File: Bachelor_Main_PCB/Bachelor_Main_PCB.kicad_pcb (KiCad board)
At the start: 4 copper layers, 216 parts, among them IC1 LD3985M18R, J1 M20-9990245, J11 F32Q-1A7H1-11022, J13 CONMHF1-SMD-G-T, J14 CONMHF1-SMD-G-T, J2 M20-9990245, J21 CONMHF1-SMD-G-T, J25 M20-9990245, J26 691137710002, J27 Conn_01x03_Pin, J28 691137710002, J29 M20-9990245, J4 MEM2075-00-140-01-A, J8 Conn_01x07_Pin, J9 M20-9990245, P1 SF70S006VBAR2000, Q1 SSM3J358R,LF, Q10 NX3008NBKW, Q11 SSM3J358R,LF, Q12 NX3008NBKW, Q13 BC817-40Q-13-F, Q2 SSM3J358R,LF, Q3 NX3008NBKW, Q4 NX3008NBKW, Q5 NX3008NBKW, Q6 NX3008NBKW, Q7 NX3008NBKW, Q8 NX3008NBKW, Q9 NX3008NBKW, U1 USB3320C-EZK-TR, U10 LMR51450FNDRRR, U11 USB2514B-I/M2, U2 STM32H7A3ZITxQ, U3 ESD7004MUTAG, U4 ESD7004MUTAG, U5 SC0683, U6 ESD7004MUTAG, U7 RC7620_1104627, U8 LM73100RPWR, U9 LMR51450FNDRRR, Y1 ECS-327TXO-30-TR, Y2 SG-210STF 24Mhz

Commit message: layouot decoupling caps to MCU
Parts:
- C22: moved to B.Cu
- moved Y2 98.3 mm to (62.8, 48.5), turned to 180 degrees
- moved L1 93.3 mm to (71.2, 52.8), turned to -90 degrees
- moved BT1 90.3 mm to (97.0, 47.0)
- moved U4 78.1 mm to (145.0, 60.5), turned to 180 degrees
- moved C24 76.4 mm to (62.5, 54.8), turned to 180 degrees
- moved C10 73.6 mm to (67.5, 51.5), turned to 180 degrees
- moved U3 73.3 mm to (139.5, 60.5), turned to 180 degrees
- moved C22 70.6 mm to (73.1, 54.0)
- moved C6 70.3 mm to (40.5, 58.0)
- moved U1 70.3 mm to (41.0, 63.0)
- moved C23 69.5 mm to (56.5, 61.0), turned to 90 degrees
- moved C9 69.1 mm to (67.5, 53.8), turned to 180 degrees
- moved C27 67.6 mm to (57.7, 51.5)
- moved C21 67.4 mm to (75.5, 54.5)
- moved C30 65.1 mm to (82.5, 56.8), turned to 90 degrees
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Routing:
- net GND: track 0.00 -> 54.3 mm, vias 0 -> 15
- net +3V5_MCU: track 0.00 -> 53.9 mm, vias 0 -> 15
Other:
- board outline added: 200 x 100 mm

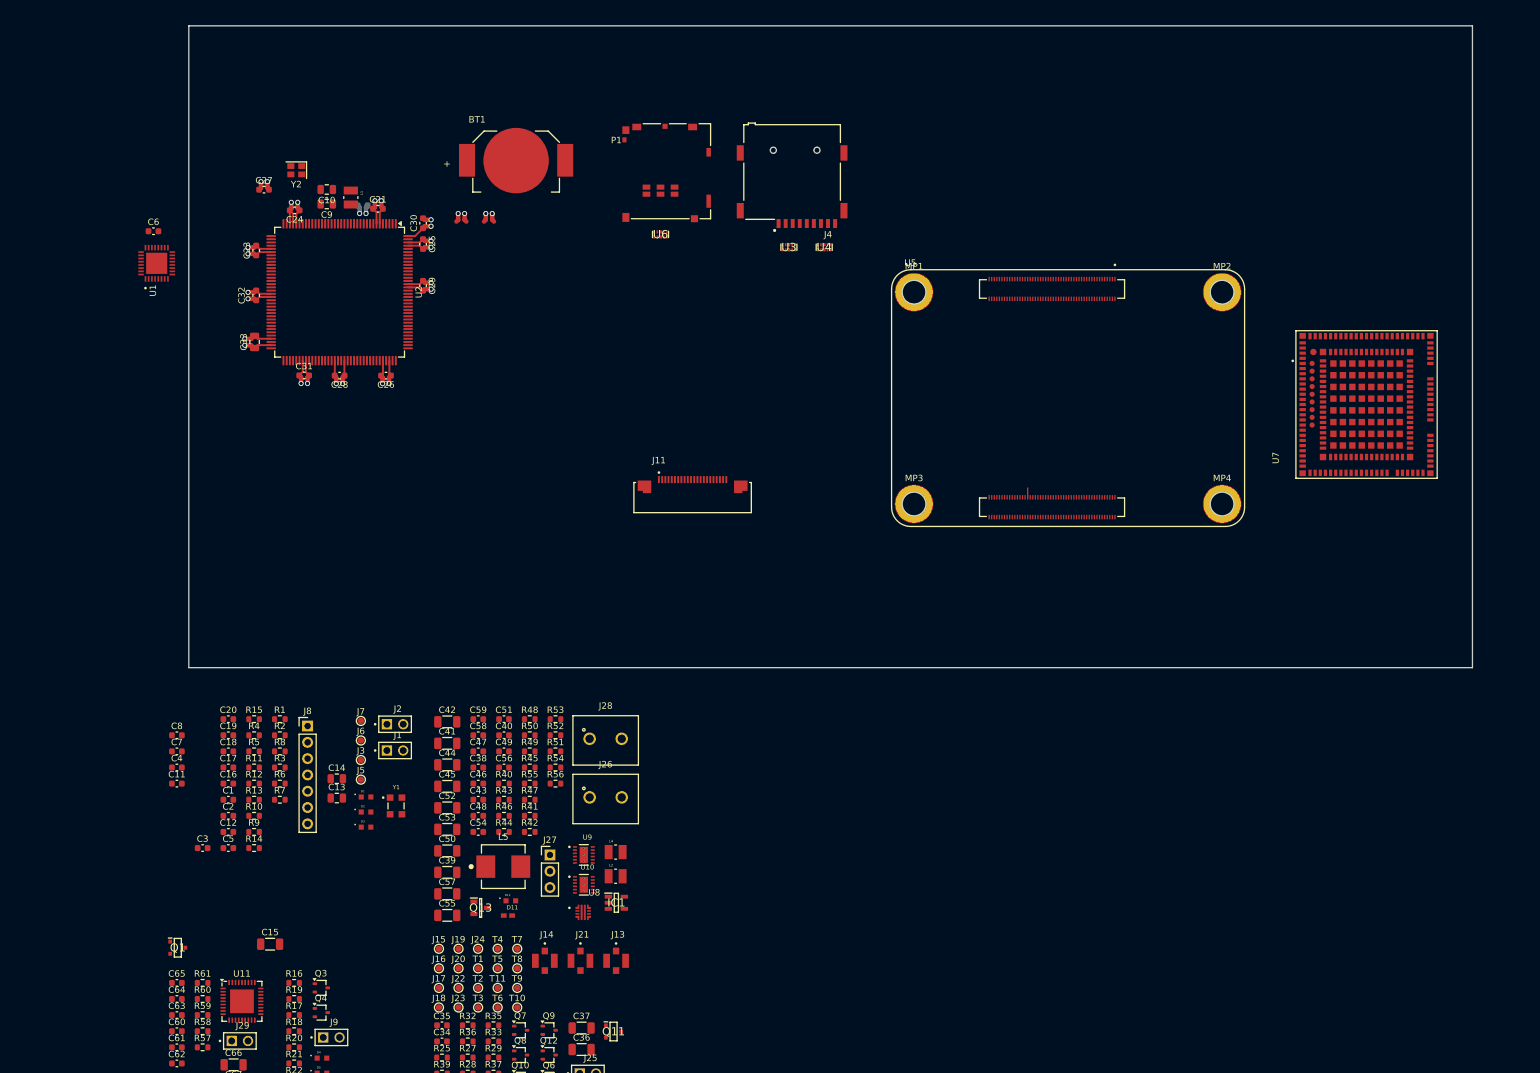
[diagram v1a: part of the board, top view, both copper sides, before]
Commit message: Rearanged components on layout
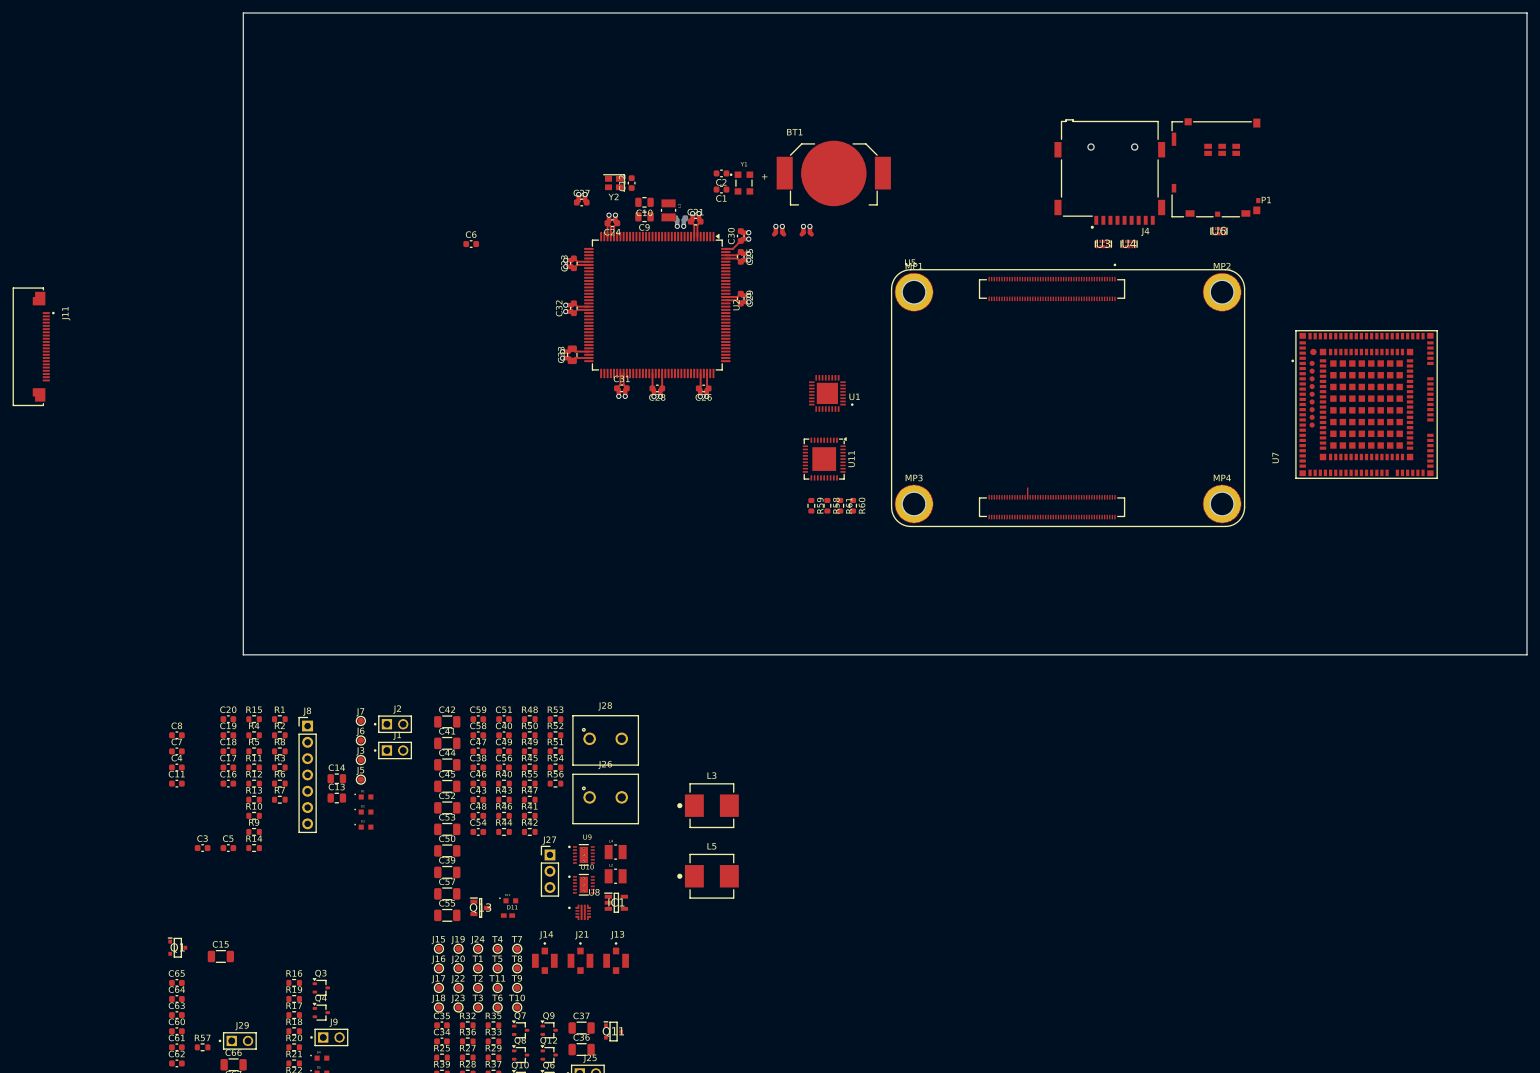
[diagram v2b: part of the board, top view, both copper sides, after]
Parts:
- added L3: 4.7uH, WE-LHMI_7050:WE-LHMI_7050, F.Cu at (127.5, 147.5)
- moved R58 127.2 mm to (145.5, 100.8), turned to -90 degrees
- moved R60 127.2 mm to (149.5, 100.8), turned to -90 degrees
- moved C2 126.2 mm to (129.0, 49.0), turned to 180 degrees
- moved R61 124.1 mm to (147.5, 100.8), turned to -90 degrees
- moved U11 124.0 mm to (145.0, 93.5), turned to -90 degrees
- moved R59 123.7 mm to (143.0, 100.8), turned to -90 degrees
- moved C1 122.2 mm to (129.0, 51.5), turned to 180 degrees
- moved C12 119.0 mm to (115.0, 50.5), turned to 90 degrees
- moved Y1 111.2 mm to (132.5, 50.5)
- moved U1 106.4 mm to (145.5, 83.3), turned to 180 degrees
- moved J11 106.1 mm to (21.0, 76.0), turned to -90 degrees
- moved P1 88.7 mm to (207.0, 55.8), turned to 180 degrees
- moved U6 87.0 mm to (206.5, 58.0)
- moved BT1 49.5 mm to (146.5, 49.0)
- moved C10 49.5 mm to (117.0, 53.5)
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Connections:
- C12 pad 1: +3V5_USB3320 -> +3V5_MCU
- Y2 pad 4: +3V5_USB3320 -> +3V5_MCU

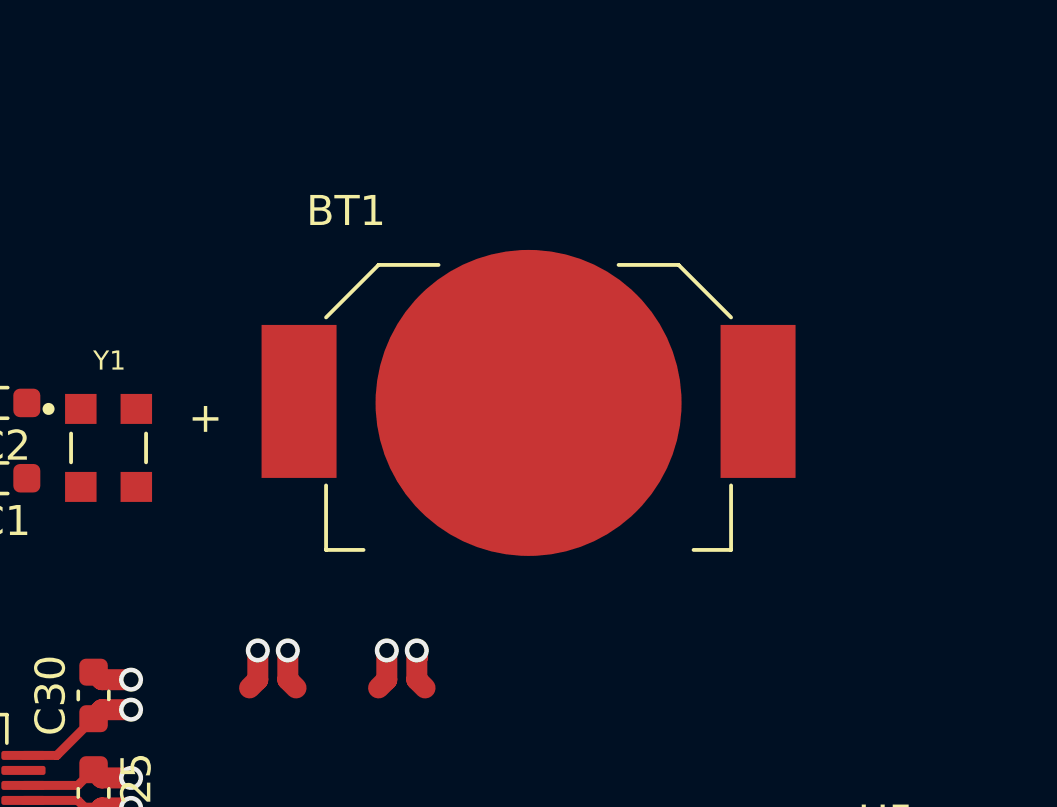
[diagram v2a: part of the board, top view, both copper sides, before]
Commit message: Rotated BAT
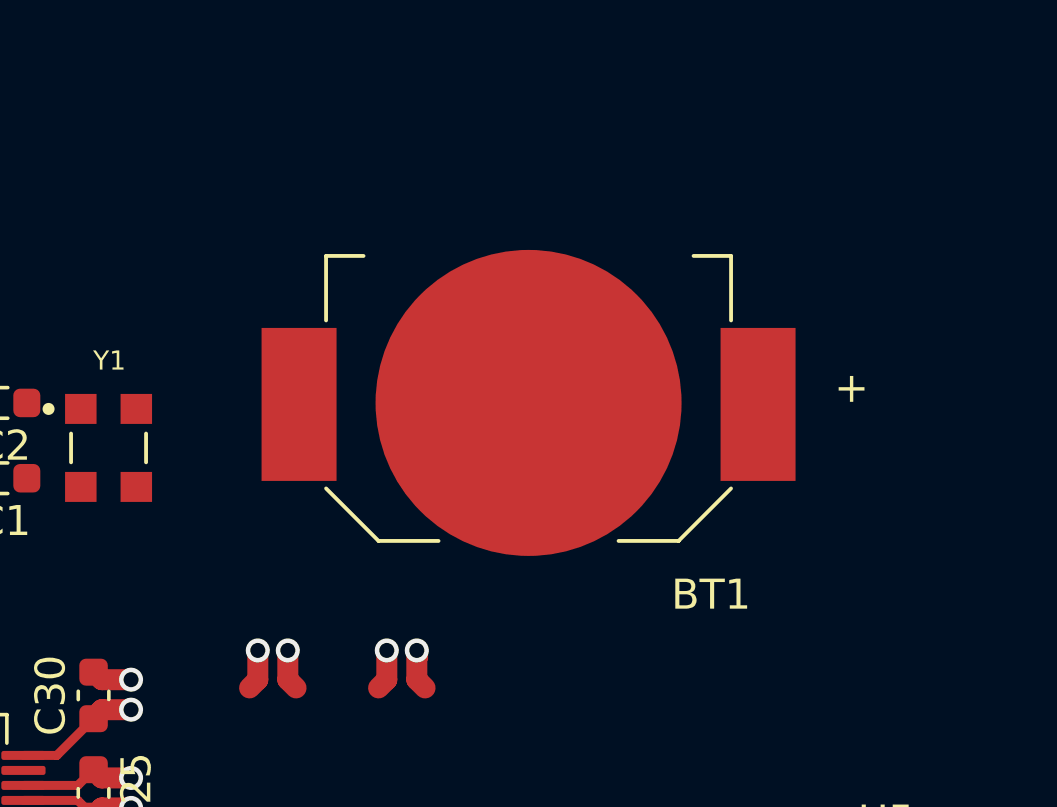
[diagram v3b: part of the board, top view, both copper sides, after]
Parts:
- turned BT1 to 180 degrees

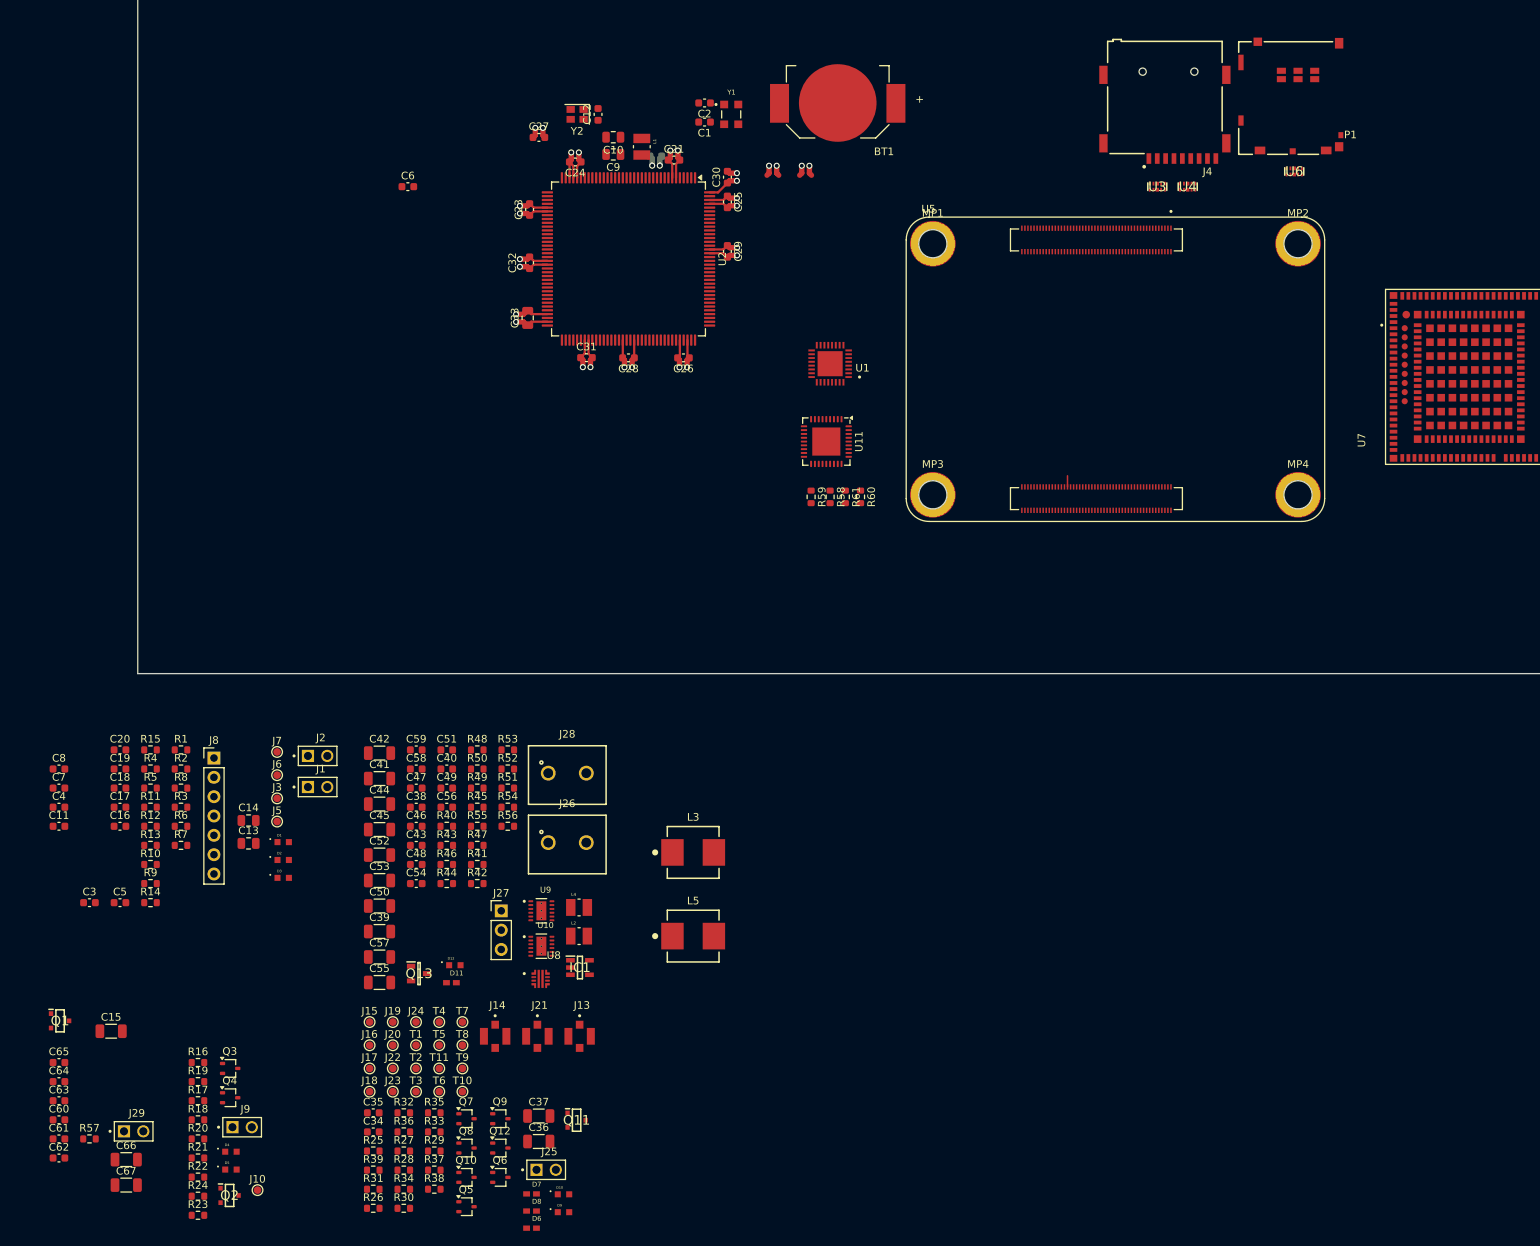
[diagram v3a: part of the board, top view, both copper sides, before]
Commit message: arrange modem components
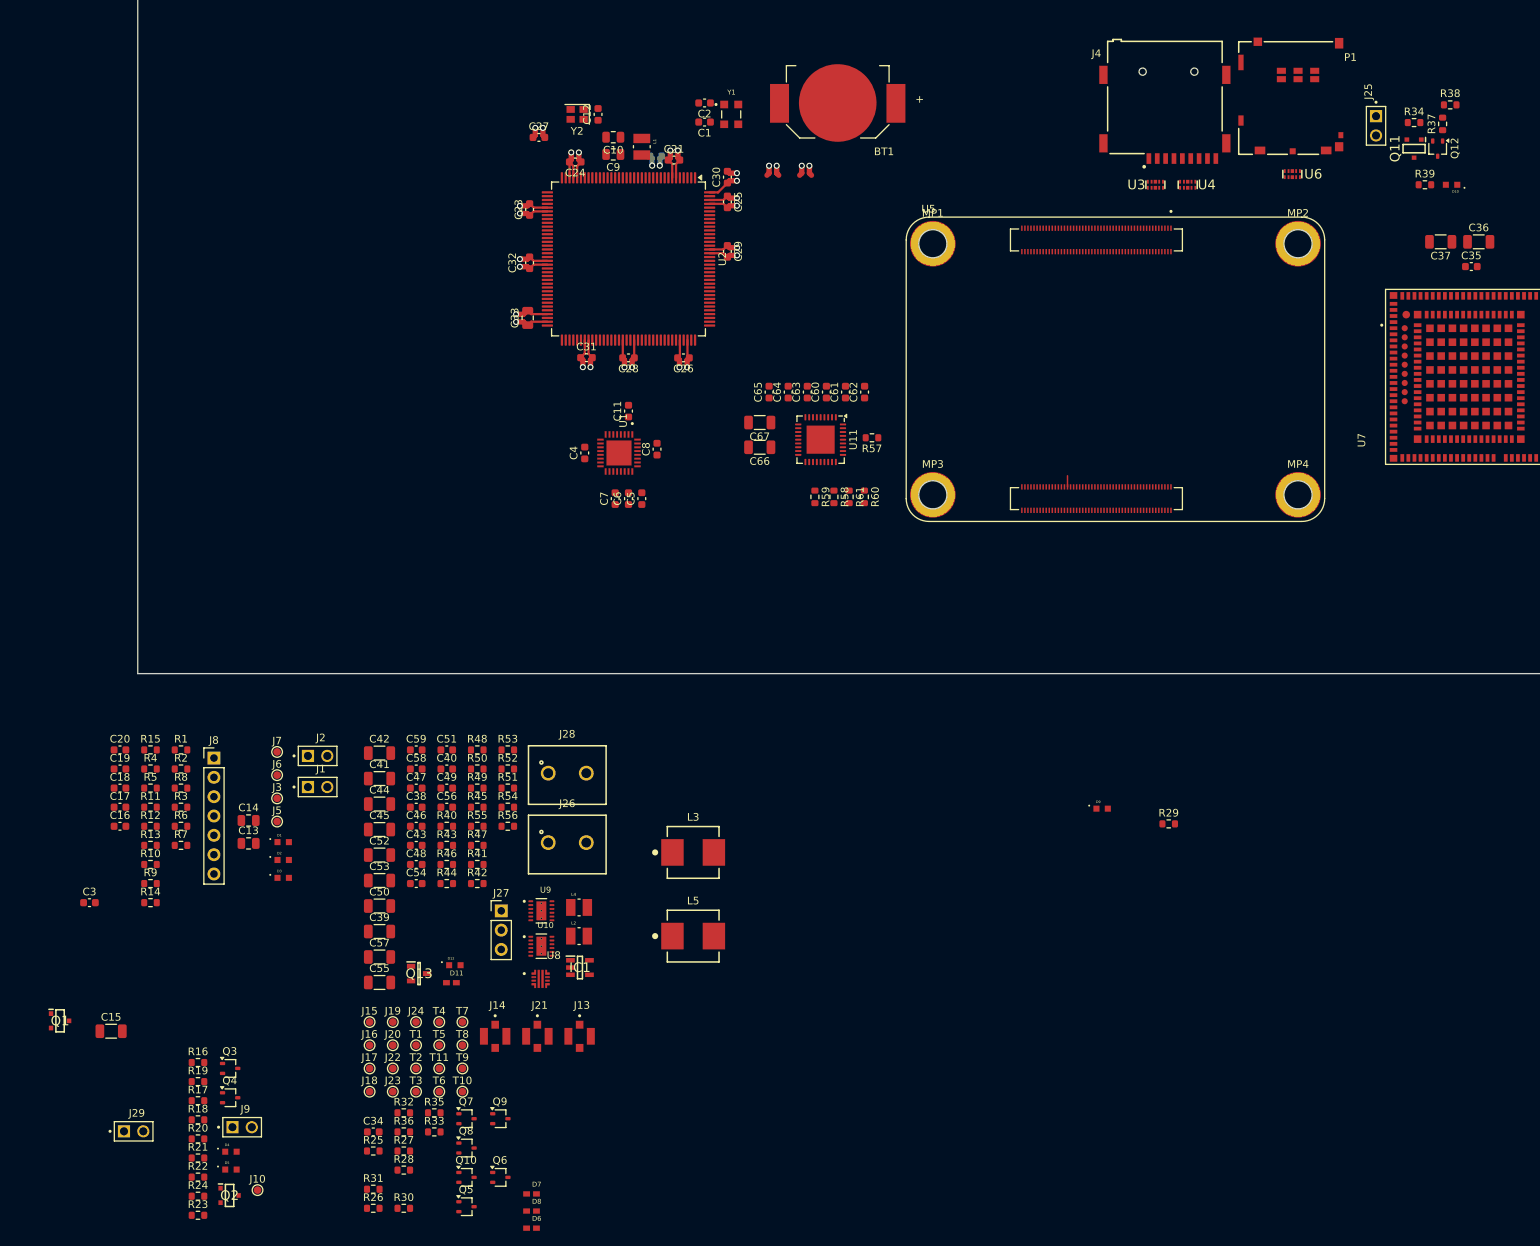
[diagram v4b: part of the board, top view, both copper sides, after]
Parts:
- moved R38 195.3 mm to (227.0, 49.2), turned to 180 degrees
- moved R34 193.1 mm to (222.2, 51.6)
- moved R37 191.0 mm to (226.0, 51.8), turned to 90 degrees
- moved R39 189.4 mm to (223.7, 59.8)
- moved C35 182.2 mm to (229.8, 70.5)
- moved Q12 180.1 mm to (225.3, 55.0), turned to -90 degrees
- moved D10 176.7 mm to (227.2, 59.8), turned to 180 degrees
- moved J25 175.3 mm to (217.2, 52.0), turned to -90 degrees
- moved C36 171.0 mm to (230.8, 67.2)
- moved Q11 168.6 mm to (222.2, 55.0), turned to -90 degrees
- moved C37 165.1 mm to (225.8, 67.2), turned to 180 degrees
- moved C62 146.1 mm to (150.0, 87.0), turned to 90 degrees
- moved C61 142.6 mm to (147.5, 87.0), turned to 90 degrees
- moved C60 139.0 mm to (145.0, 87.0), turned to 90 degrees
- moved R57 138.1 mm to (151.0, 93.0), turned to 180 degrees
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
